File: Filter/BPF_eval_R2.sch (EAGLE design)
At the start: 7 parts, among them J1 142-0711-821, J2 142-0711-821, J3 142-0711-821, J4 142-0711-821, U1 885071-A

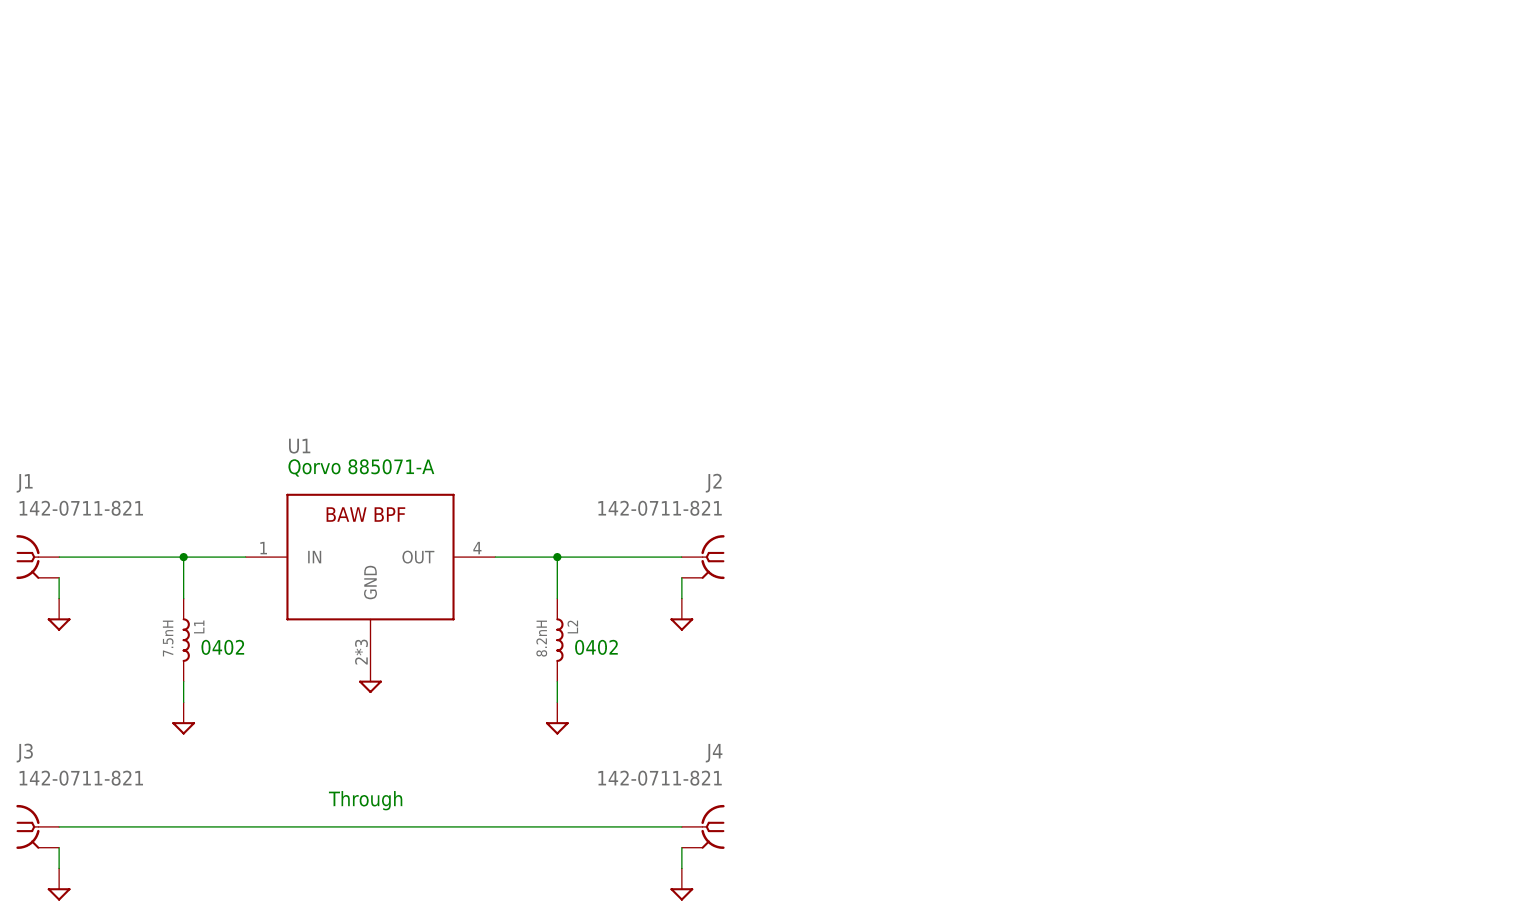
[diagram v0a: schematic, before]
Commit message: Fixed Nathan's filter board. Mostly EAGLE stupidity problems. - Switched SMA connectors to the PSAS standard. - Switched grid to 10 mil because OCD. - Loaded OSH Park 2 layer DRC. - Made "RF" class to keep away the ground plane. - Fixed vias (were only layer 1-2, not 1-16). - Added text. Should be good to go?
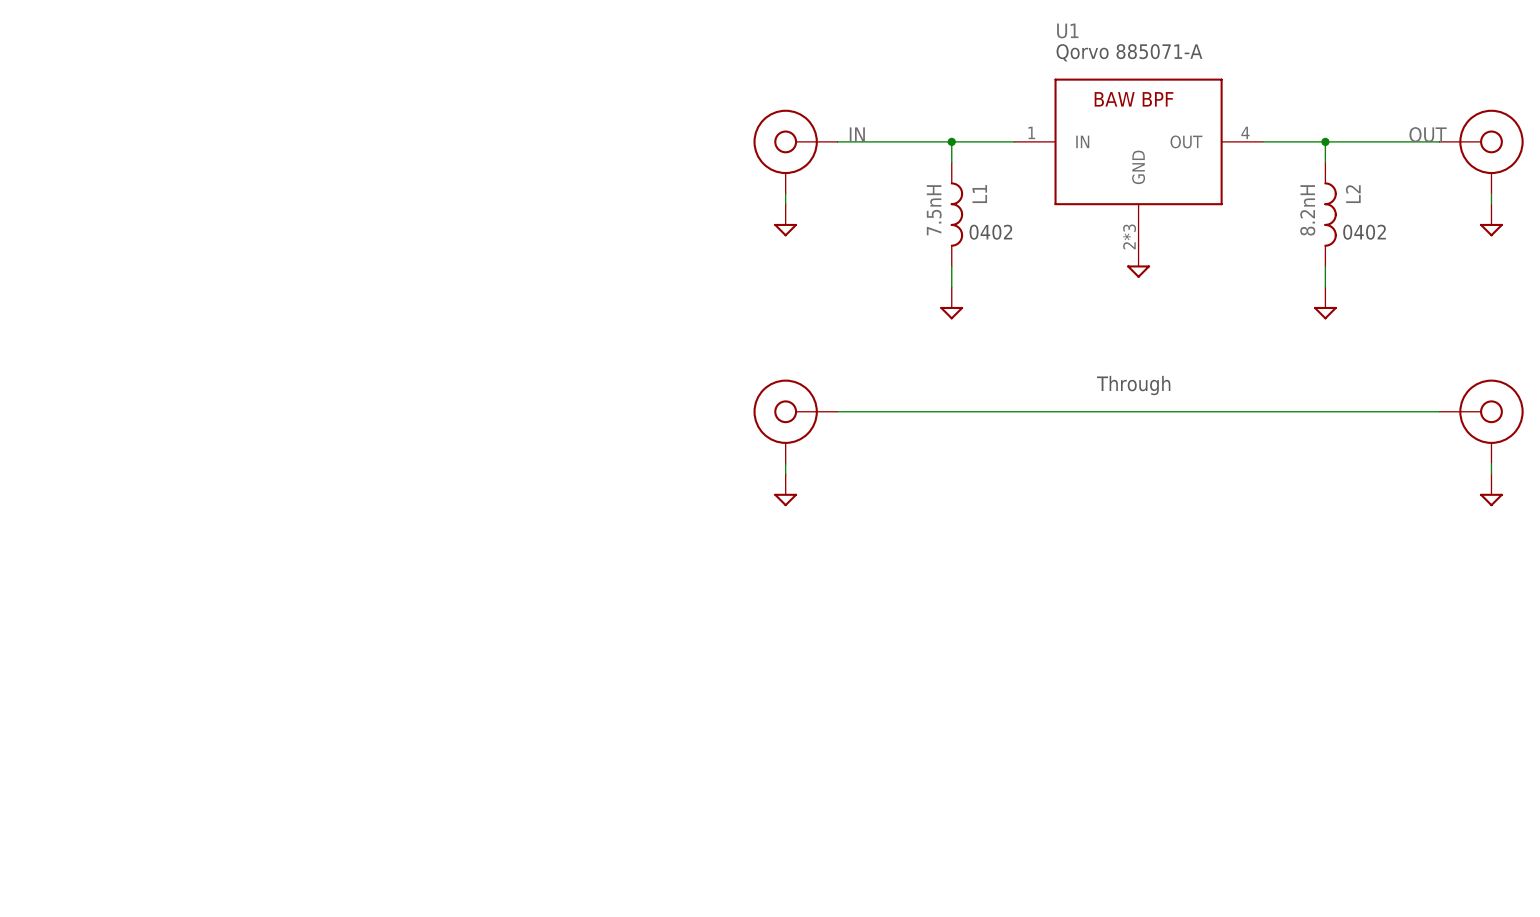
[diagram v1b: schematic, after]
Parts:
- removed J1, J2, J3, J4: 142-0711-821, con-coax:SMA-142-0711-821/826
- added CF1, CF2, CF3, CF4: SMA-CINCH-END-FIRE, psas_c3_team05:SMA-CINCH-END-FIRE
- L1, L2: device Seeed-Inductor:SMD-INDUCTOR-3.3NH-0.3NH-300MA(0402) -> rcl_custom:L-US0402-B-NOSILK
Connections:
- removed net N$1: J1.1, L1.1, U1.IN
- removed net N$2: J2.1, L2.1, U1.OUT
- removed net N$3: J3.1, J4.1
- new net IN: CF1.CENTERCONDUCTOR, L1.1, U1.IN
- new net OUT: CF3.CENTERCONDUCTOR, L2.1, U1.OUT
- new net THROUGH: CF2.CENTERCONDUCTOR, CF4.CENTERCONDUCTOR
- net GND: now also CF1.GND, CF2.GND, CF3.GND, CF4.GND; no longer J1.2, J2.2, J3.2, J4.2
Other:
- moved on the sheet: U1
